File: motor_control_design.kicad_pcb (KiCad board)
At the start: 2 copper layers, 57.1 x 57.2 mm, 97 parts, among them J1 TYPE-C-31-M-12, J10 5V, J2 SWD, J3 VBAT, J4 GND, J5 FC_M/P, J6 Conn_01x06, J7 Conn_01x04_Pin, J8 Conn_01x06, J9 GND, Q1 RF1S9540SM, Q10 2N7002, Q11 2N7002, Q12 2N7002, Q13 2N7002, Q14 RF1S9540SM, Q15 IRLZ44NS, Q16 2N7002, Q2 RF1S9540SM, Q3 IRLZ44NS, Q4 2N7002, Q5 2N7002, Q6 RF1S9540SM, Q7 IRLZ44NS, Q8 2N7002, Q9 IRLZ44NS, U1 STM32F401CCU6, U2 LT1962-3.3, U3 LTC4365DDB, U4 TPS563200, U5 SSM6N7002KFU_LF, Y1 16MHz

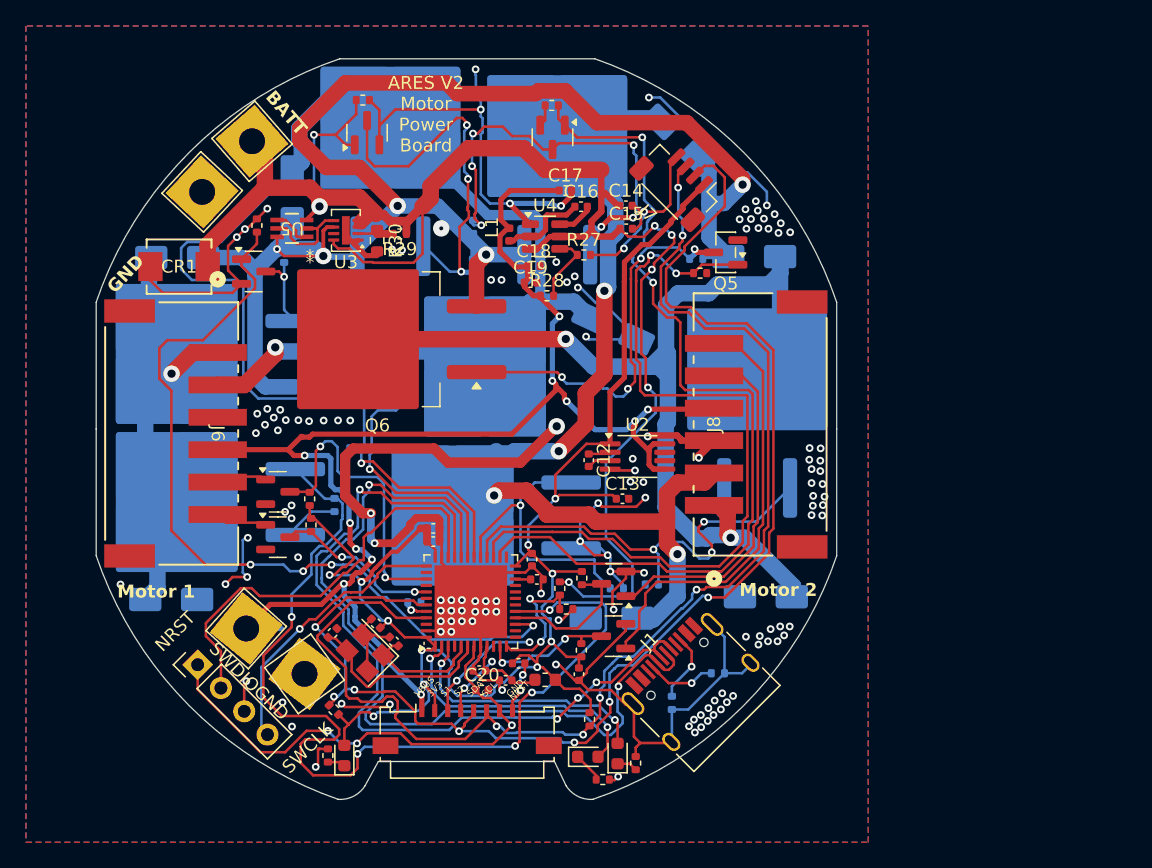
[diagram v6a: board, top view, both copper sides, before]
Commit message: small changes
fixed some ground plane connections, messed with the usbc footprint
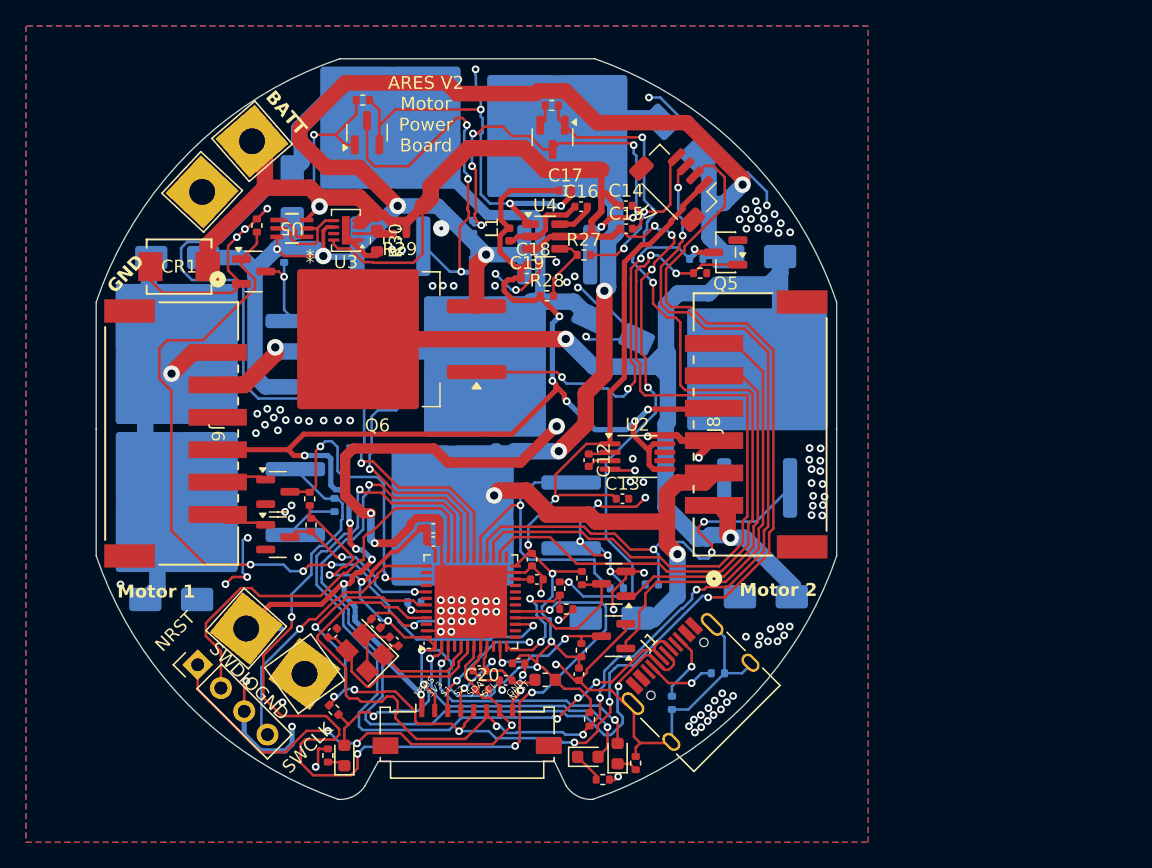
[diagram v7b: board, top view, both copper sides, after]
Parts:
- J1: footprint Connector_USB:USB_C_Receptacle_HRO_TYPE-C-31-M-12 -> CustomARES:USB_C_Receptacle_HRO_TYPE-C-31-M-12--MODIFIED
- moved C19 0.44 mm to (153.7, 77.5)
- moved C18 0.12 mm to (154.2, 76.4)
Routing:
- net GND: track 252.0 -> 266.8 mm, vias 137 -> 140
- net +5V: track 113.2 -> 116.5 mm

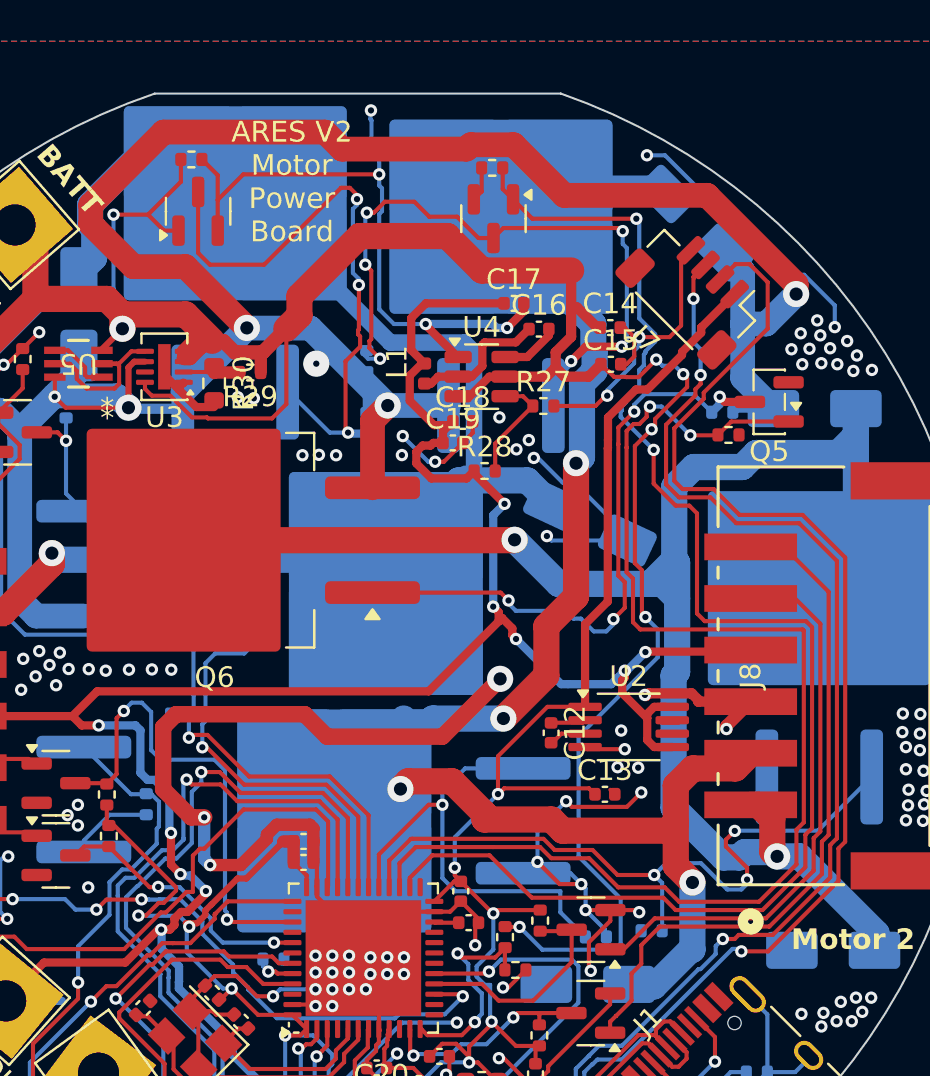
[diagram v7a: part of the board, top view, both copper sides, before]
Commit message: board edge tweaks
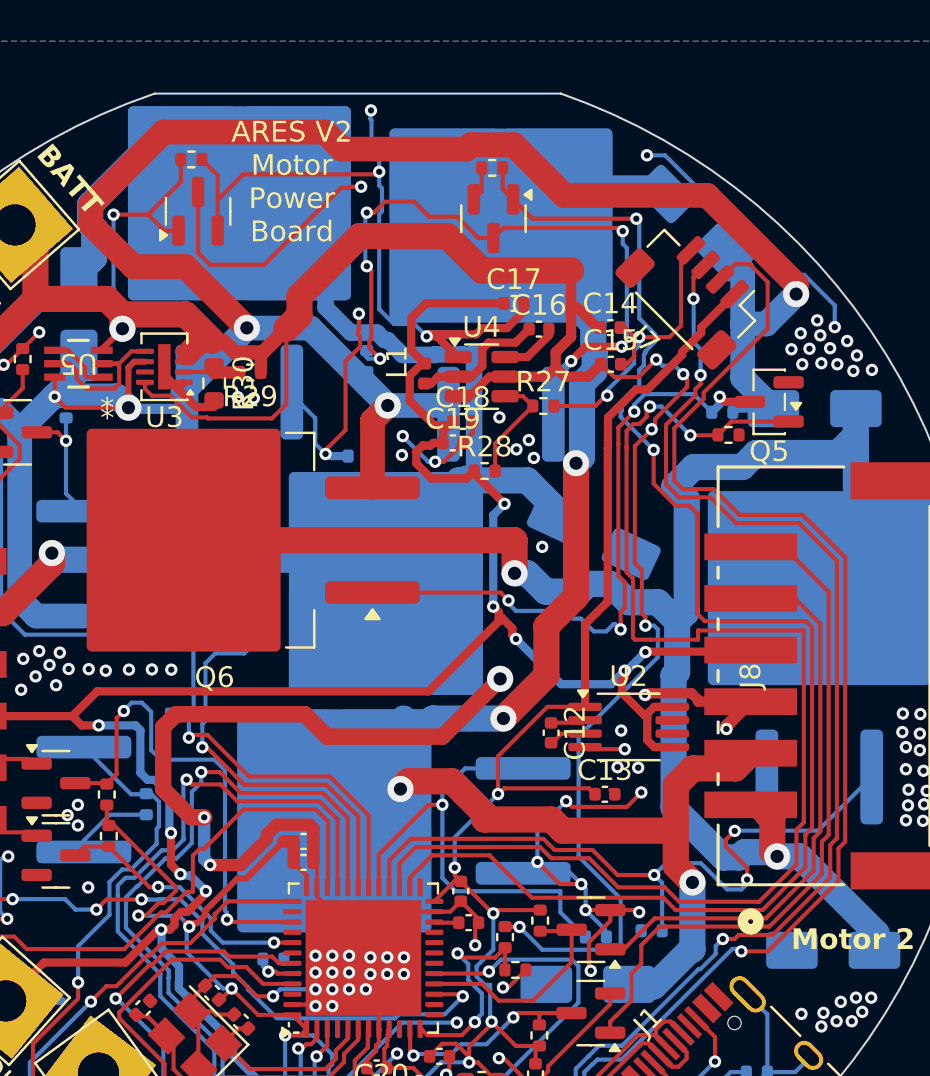
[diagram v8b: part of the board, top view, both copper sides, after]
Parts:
- moved R14 1.65 mm to (149.1, 78.1), turned to 0 degrees
- moved D6 0.68 mm to (160.5, 82.0)
- moved Q14 0.42 mm to (156.0, 68.4)
- moved Q1 0.20 mm to (143.3, 67.3)
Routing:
- net GND: track 266.8 -> 258.3 mm, vias 140 -> 136
- net Net-(Q1-G): track 29.2 -> 25.0 mm
- net /M2Q1: track 61.3 -> 62.4 mm
- net VMOTOR: track 124.6 -> 125.4 mm, vias 6 -> 5
- net /M1B: track 58.4 -> 59.1 mm
- net Net-(Q5-D): track 30.8 -> 31.4 mm
